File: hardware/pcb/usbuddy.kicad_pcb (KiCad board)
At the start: 2 copper layers, 14.1 x 62.1 mm, 14 parts, among them J1 USB_A, SW1 SW_Push, U1 CH552G, U2 ER_OLEDM0.91_1x-I2C

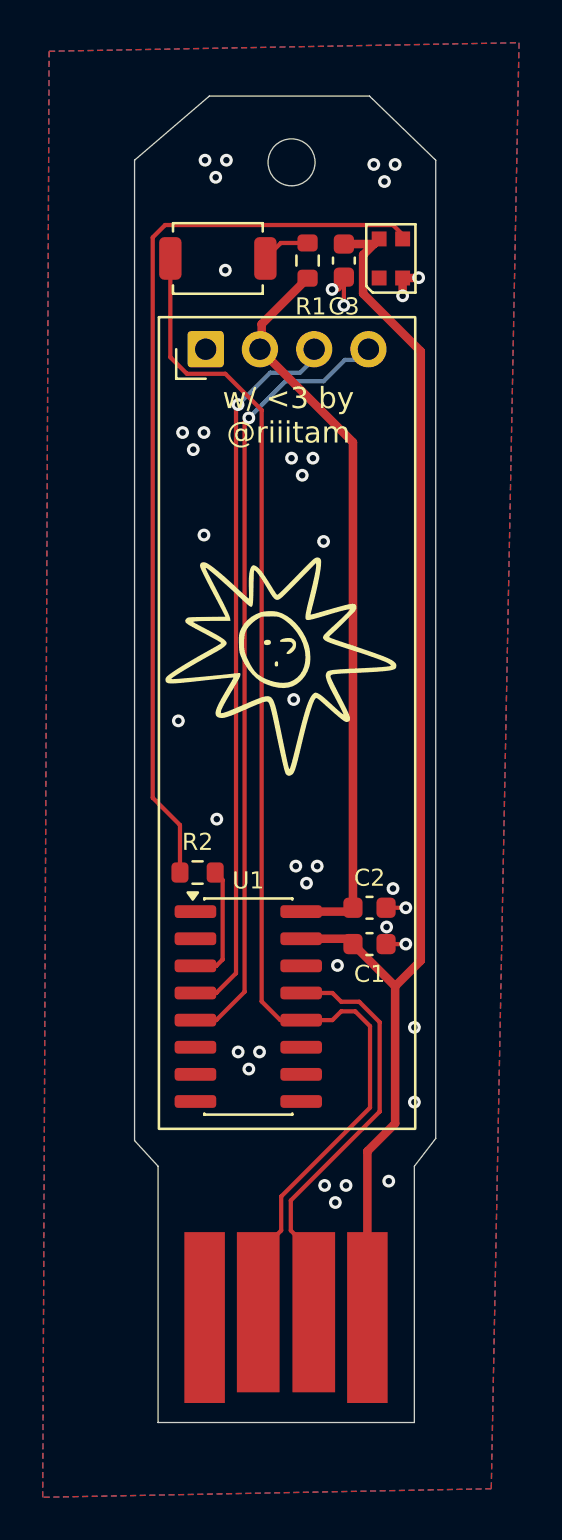
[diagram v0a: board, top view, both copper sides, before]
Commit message: update design to use green static LED
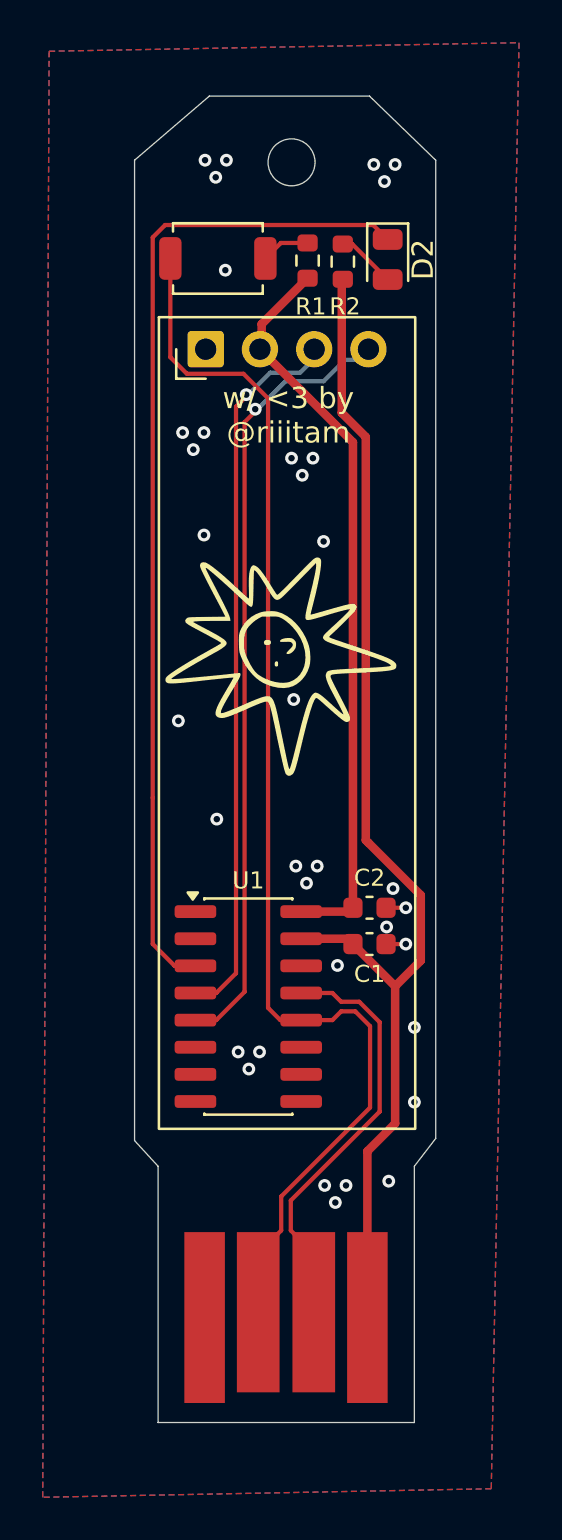
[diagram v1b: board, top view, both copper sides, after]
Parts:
- removed C3: 100n, Capacitor_SMD:C_0603_1608Metric
- removed D1: WS2812B-2020, LED_SMD:LED_WS2812B-2020_PLCC4_2.0x2.0mm
- added D2: KT-0805G, LED_SMD:LED_0805_2012Metric, F.Cu at (149.1, 72.1)
- R2: value 470 -> 1k
- moved R2 29.4 mm to (147.0, 72.2), turned to 90 degrees
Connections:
- R2 pad 1: NEOPX -> VBUS
- R2 pad 2: Net-(U1-P1.5) -> Net-(D2-A)
- U1 pad 3: Net-(U1-P1.5) -> LED
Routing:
- net LED: track 0.00 -> 47.0 mm
- net NEOPX: track 42.6 -> 0.00 mm
- net Net-(U1-P1.5): track 5.96 -> 0.00 mm
- net GND: track 5.74 -> 1.85 mm, vias 39 -> 35
- net VBUS: track 62.6 -> 59.1 mm
- net Net-(D2-A): track 0.00 -> 2.79 mm
